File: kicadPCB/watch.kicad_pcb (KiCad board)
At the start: 2 copper layers, 81 x 53 mm, 64 parts, among them IC1 ISL1209, J2 USB-MICROB, M1 BOS_LIBS_SWD_BREAKOUTS, T1 BC850, U2 MKL27Z256VLH4, Y1 Crystal

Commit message: fixed compass orientation
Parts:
- moved U$1 3.06 mm to (116.8, 102.9), turned to 90 degrees
- moved COMPCAP46 1.53 mm to (116.8, 96.5), turned to 180 degrees
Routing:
- net /PTC8: track 44.3 -> 73.1 mm
- net /PTC9: track 45.7 -> 67.6 mm
- net GND: track 198.5 -> 181.9 mm, vias 14 -> 12
- net /N$1: track 9.93 -> 9.39 mm
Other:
- board text removed: "FillOverPAD:GND:22:348"

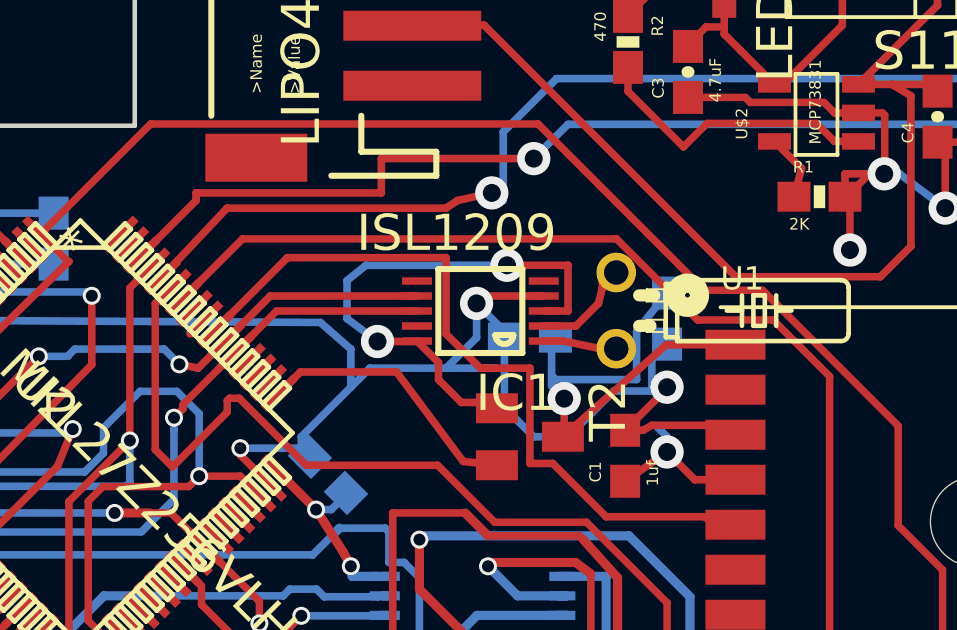
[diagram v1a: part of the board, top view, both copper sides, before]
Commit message: fixed clock crystal
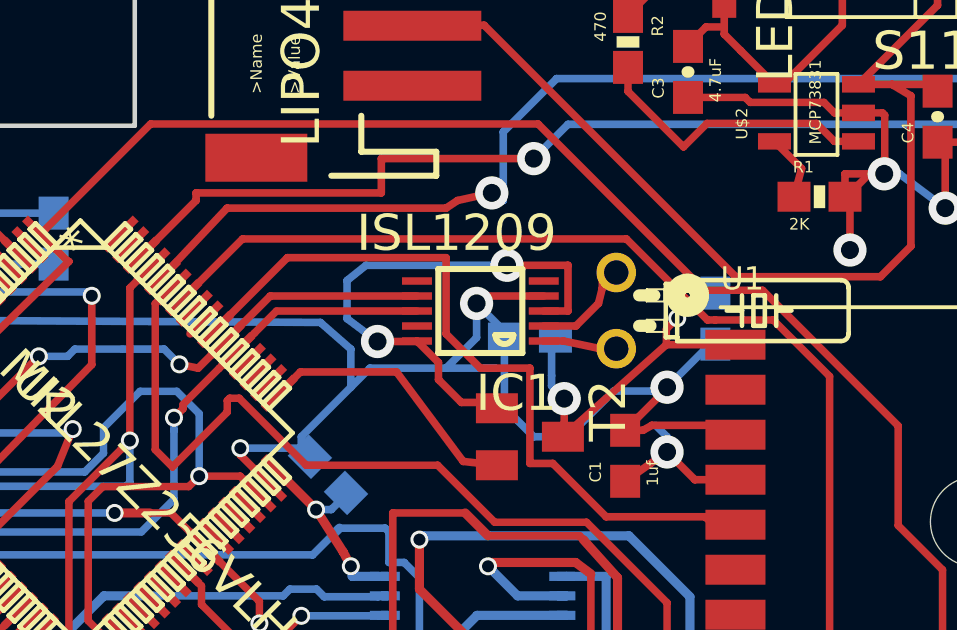
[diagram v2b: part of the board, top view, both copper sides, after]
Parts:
- moved C9 1.61 mm to (168.9, 92.7)
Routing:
- net /N$6: track 16.8 -> 13.3 mm, vias 1 -> 2

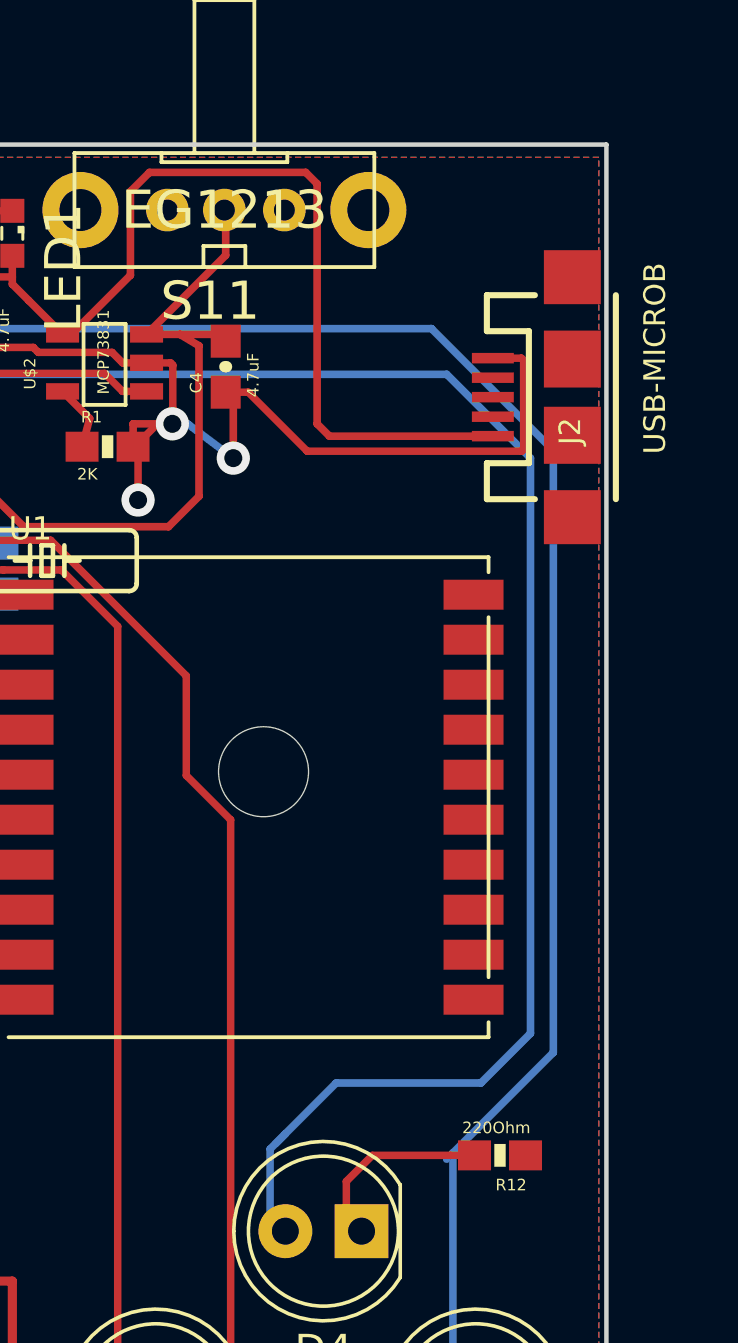
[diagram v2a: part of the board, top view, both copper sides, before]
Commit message: added through hole usb
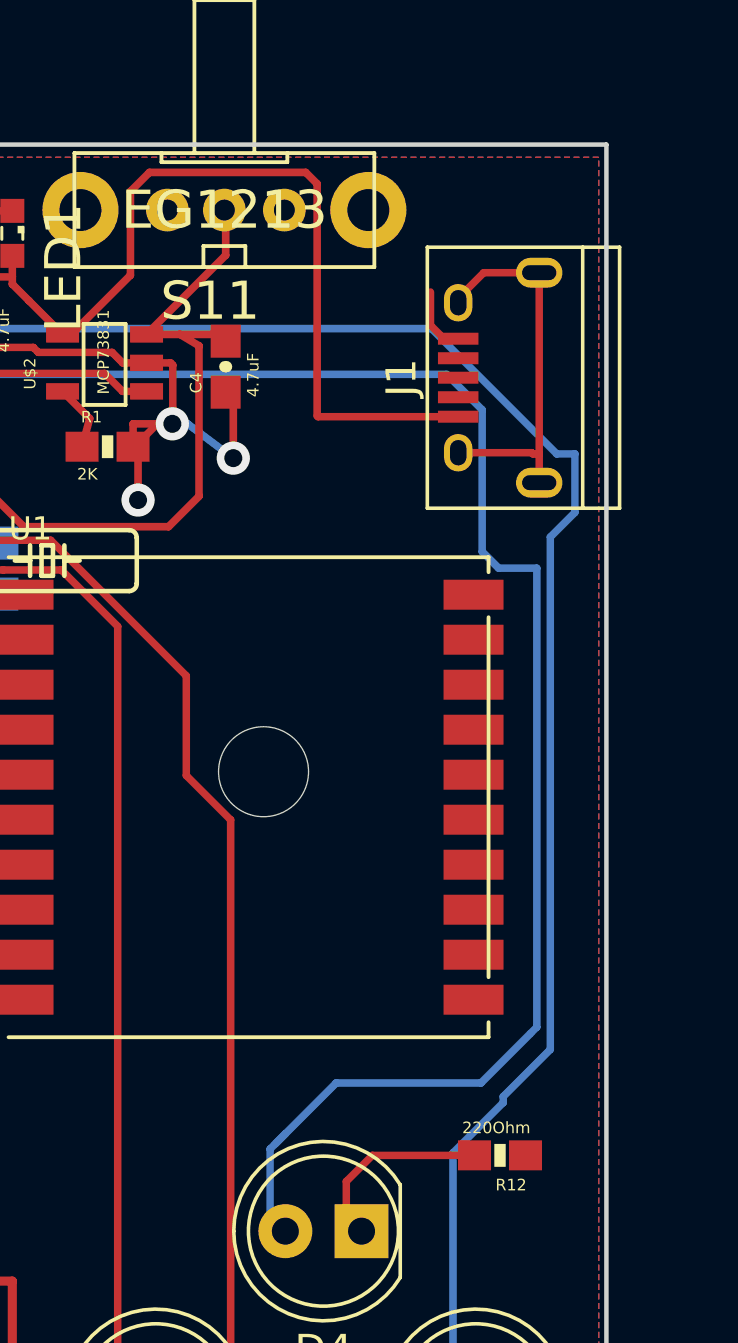
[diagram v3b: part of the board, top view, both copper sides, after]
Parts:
- removed J2: USB-MICROB, USB-MICROB
- added J1: USB_OTG, Connectors:USB_Micro-B, F.Cu at (185.4, 86.4)
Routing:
- net Net-(J1-Pad6): track 0.00 -> 12.9 mm
- net GND: track 182.4 -> 169.8 mm
- net /N$4: track 31.4 -> 29.8 mm
- net /PTD5: track 72.6 -> 73.6 mm
- net /PTD3: track 76.1 -> 76.8 mm

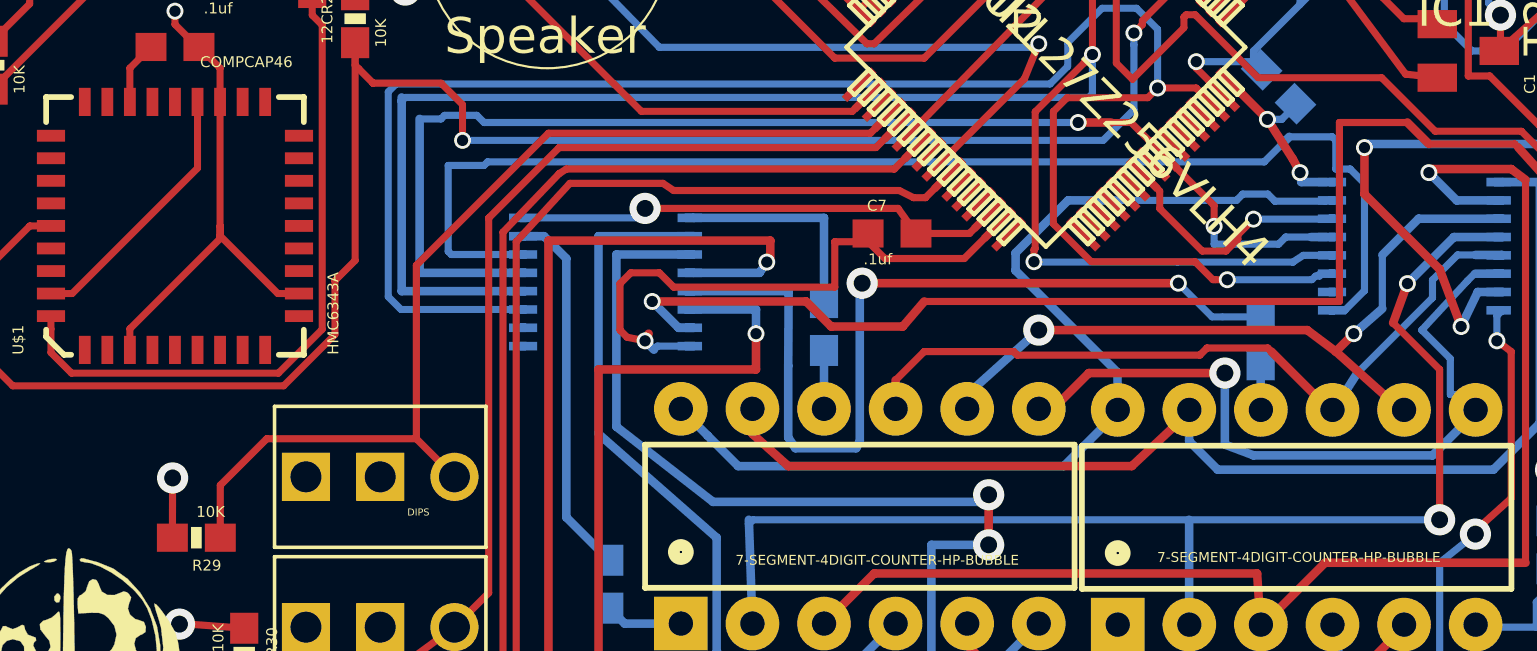
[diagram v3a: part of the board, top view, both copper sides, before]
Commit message: fixed bad reset on SRs
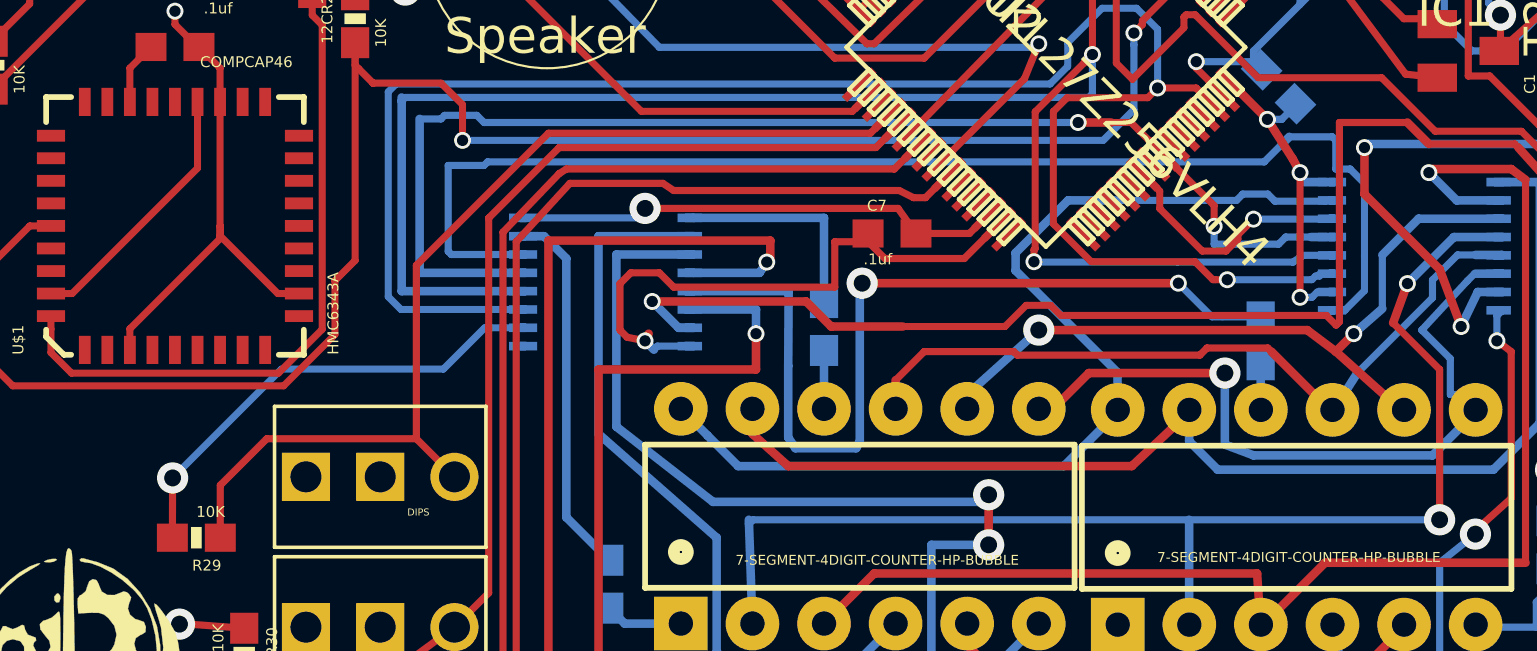
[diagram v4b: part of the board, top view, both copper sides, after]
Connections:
- U$4 pad MR: Net-(U$4-PadMR) -> V+
- U$5 pad MR: Net-(U$5-PadMR) -> V+
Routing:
- net V+: track 110.1 -> 129.6 mm, vias 17 -> 18
- net /N$29: track 53.8 -> 54.7 mm

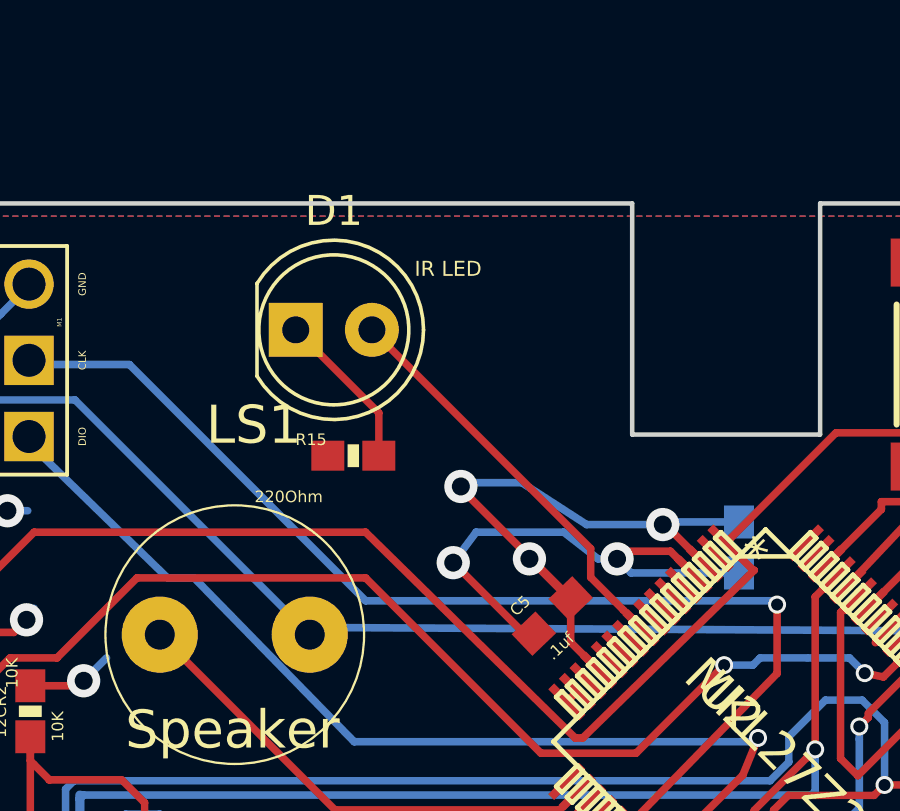
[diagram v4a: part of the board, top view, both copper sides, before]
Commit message: reversed IR LED
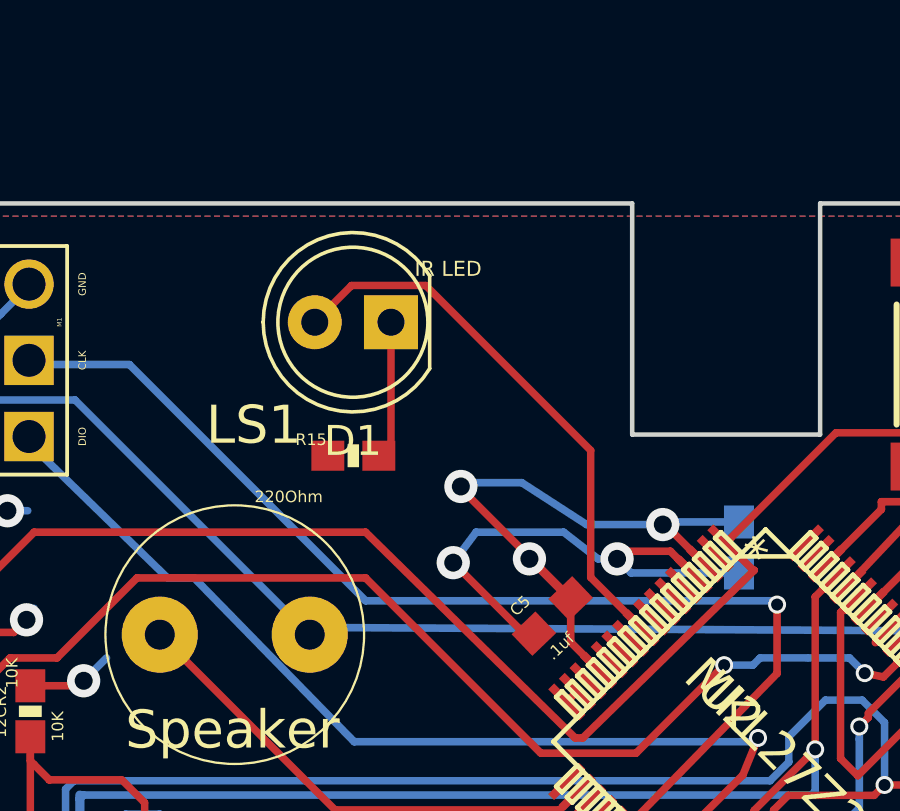
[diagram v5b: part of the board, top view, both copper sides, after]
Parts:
- moved D1 3.19 mm to (135.3, 82.5), turned to 180 degrees
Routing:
- net /PTE20: track 13.6 -> 18.6 mm
- net /N$39: track 5.34 -> 4.67 mm
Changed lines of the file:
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@@
     (links 159)
     (no_connects 0)
-    (area 107.917149 78.430582 189.085051 131.576618)
+    (area 107.917149 73.510799 191.505 131.576618)
     (thickness 1.6)
     (drawings 84)
-    (tracks 861)
+    (tracks 863)
     (zones 0)
     (modules 64)
@@
   )
   (module LEDs:LED_D5.0mm (layer Top)
-    (at 132.08 82.804)
+    (at 135.255 82.55 180)
     (descr "LED, diameter 5.0mm, 2 pins, http://cdn-reichelt.de/documents/datenblatt/A500/LL-504BC2E-009.pdf")
     (tags "LED diameter 5.0mm 2 pins")
-    (fp_text reference D1 (at 1.27 -3.96) (layer F.SilkS)
+    (fp_text reference D1 (at 1.27 -3.96 180) (layer F.SilkS)
       (effects (font (size 1 1) (thickness 0.15)))
     )
-    (fp_text value LED (at 1.27 3.96) (layer F.Fab)
+    (fp_text value LED (at 1.27 3.96 180) (layer F.Fab)
       (effects (font (size 1 1) (thickness 0.15)))
     )
@@
     (fp_line (start 4.5 3.25) (end 4.5 -3.25) (layer F.CrtYd) (width 0.05))
     (fp_line (start 4.5 -3.25) (end -1.95 -3.25) (layer F.CrtYd) (width 0.05))
-    (pad 1 thru_hole rect (at 0 0) (size 1.8 1.8) (drill 0.9) (layers *.Cu *.Mask)
+    (pad 1 thru_hole rect (at 0 0 180) (size 1.8 1.8) (drill 0.9) (layers *.Cu *.Mask)
       (net 49 /N$39))
-    (pad 2 thru_hole circle (at 2.54 0) (size 1.8 1.8) (drill 0.9) (layers *.Cu *.Mask)
+    (pad 2 thru_hole circle (at 2.54 0 180) (size 1.8 1.8) (drill 0.9) (layers *.Cu *.Mask)
       (net 86 /PTE20))
     (model LEDs.3dshapes/LED_D5.0mm.wrl
@@
   (segment (start 173.768411 123.037589) (end 175.26 121.546) (width 0.25) (layer Top) (net 48))
   (segment (start 175.26 121.546) (end 175.26 120.396) (width 0.25) (layer Top) (net 48))
-  (segment (start 134.85 87) (end 134.85 85.574) (width 0.25) (layer Top) (net 49))
-  (segment (start 134.85 85.574) (end 132.08 82.804) (width 0.25) (layer Top) (net 49))
+  (segment (start 135.255 82.55) (end 135.255 86.595) (width 0.25) (layer Top) (net 49))
+  (segment (start 135.255 86.595) (end 134.85 87) (width 0.25) (layer Top) (net 49))
+  (segment (start 134.8 87) (end 134.85 87) (width 0.25) (layer Top) (net 49))
   (segment (start 112.86 92.964) (end 112.86 87.481345) (width 0.25) (layer Top) (net 50))
   (segment (start 112.86 87.481345) (end 111.791244 86.412589) (width 0.25) (layer Top) (net 50))
@@
   (segment (start 159.936244 93.231589) (end 161.079244 94.374589) (width 0.254) (layer Top) (net 69))
   (segment (start 161.079244 94.374589) (end 162.730244 94.374589) (width 0.254) (layer Top) (net 69))
-  (segment (start 134.62 82.804) (end 141.912243 90.096243) (width 0.25) (layer Top) (net 86))
-  (segment (start 141.912243 90.096243) (end 141.912243 91.055124) (width 0.25) (layer Top) (net 86))
-  (segment (start 141.912243 91.055124) (end 142.998431 92.141312) (width 0.25) (layer Top) (net 86))
-  (segment (start 142.998431 92.141312) (end 143.589996 92.732877) (width 0.25) (layer Top) (net 86))
+  (segment (start 132.715 82.55) (end 133.940001 81.324999) (width 0.25) (layer Top) (net 86))
+  (segment (start 133.940001 81.324999) (end 136.415001 81.324999) (width 0.25) (layer Top) (net 86))
+  (segment (start 136.415001 81.324999) (end 141.912243 86.822241) (width 0.25) (layer Top) (net 86))
+  (segment (start 141.912243 86.822241) (end 141.912243 91.055124) (width 0.25) (layer Top) (net 86))
+  (segment (start 141.912243 91.055124) (end 143.589996 92.732877) (width 0.25) (layer Top) (net 86))
   (segment (start 141.115109 95.207764) (end 141.468663 94.85421) (width 0.25) (layer Top) (net 91))
   (segment (start 127.54864 92.964) (end 133.389173 98.804533) (width 0.25) (layer Top) (net 93))
